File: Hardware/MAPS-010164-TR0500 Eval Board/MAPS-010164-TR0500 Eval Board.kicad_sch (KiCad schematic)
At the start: 13 parts, among them IC1 MAPS-010164-TR0500, J1 Conn_Coaxial, J2 Conn_Coaxial, J3 Conn_02x02_Top_Bottom, J4 Conn_02x02_Top_Bottom, J5 Conn_02x04_Top_Bottom, J6 Conn_Coaxial, J7 Conn_Coaxial, J8 Conn_02x02_Top_Bottom

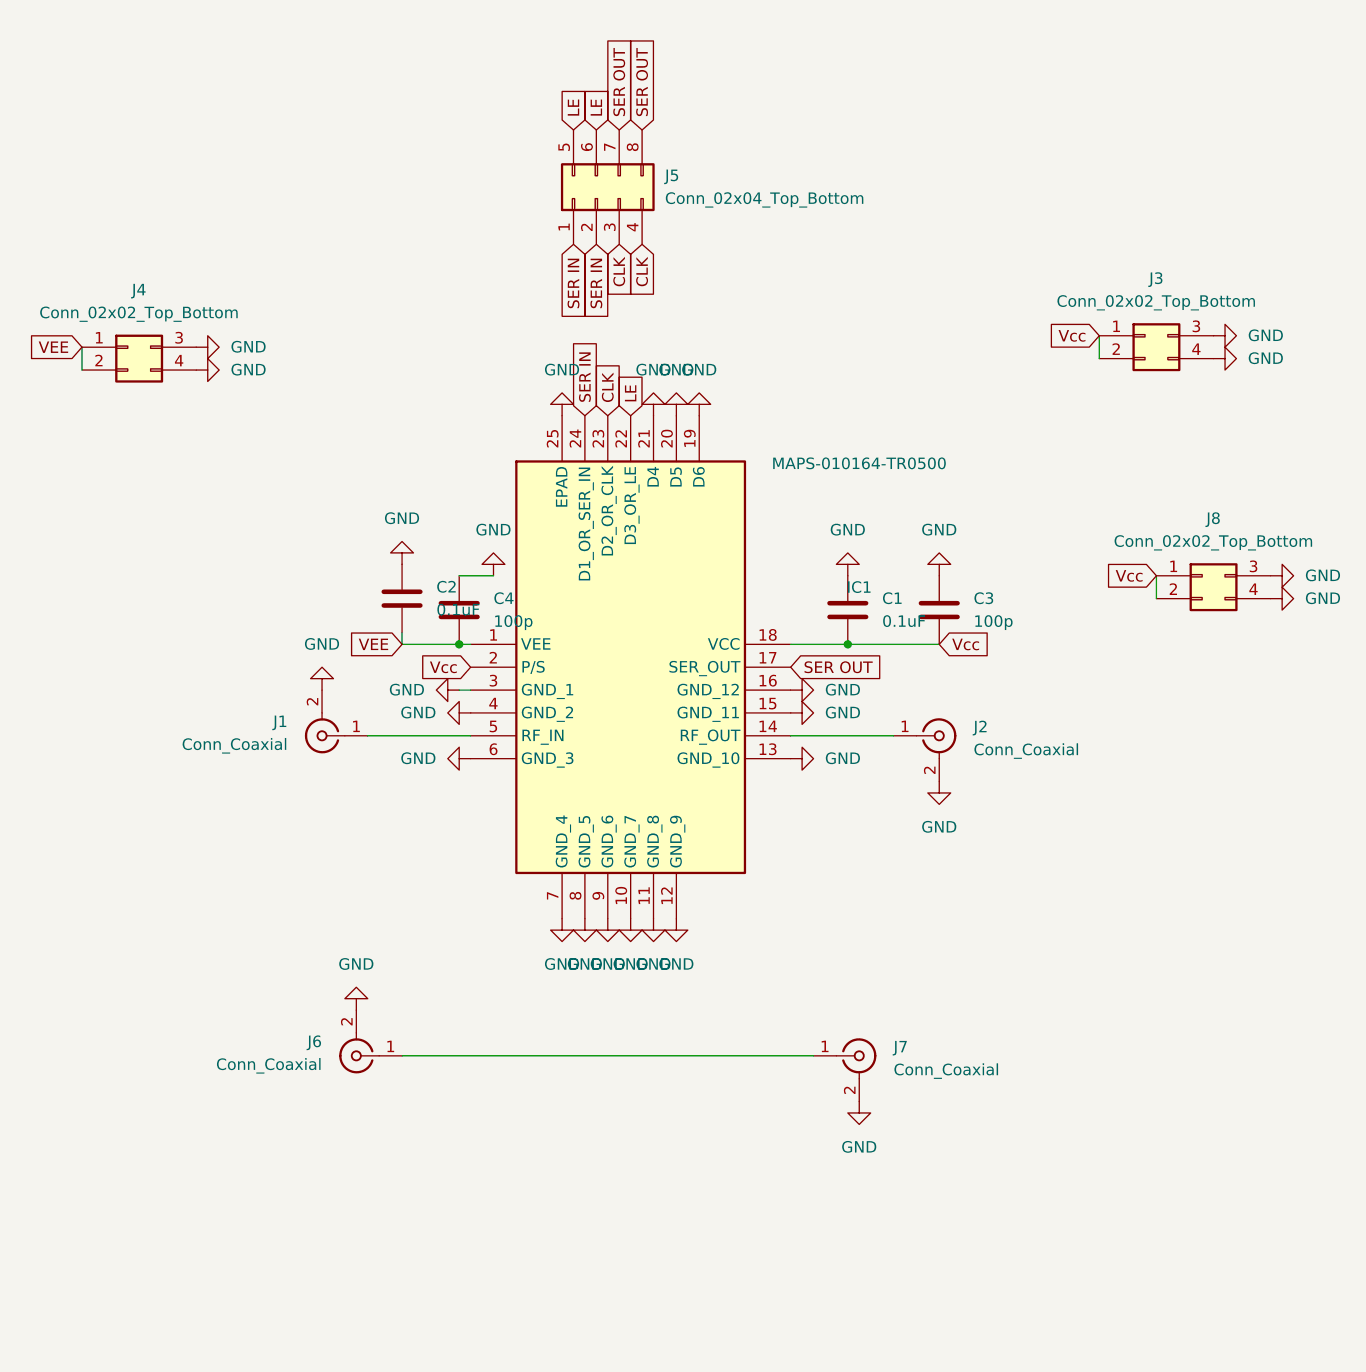
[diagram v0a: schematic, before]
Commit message: Digital Line Filtering
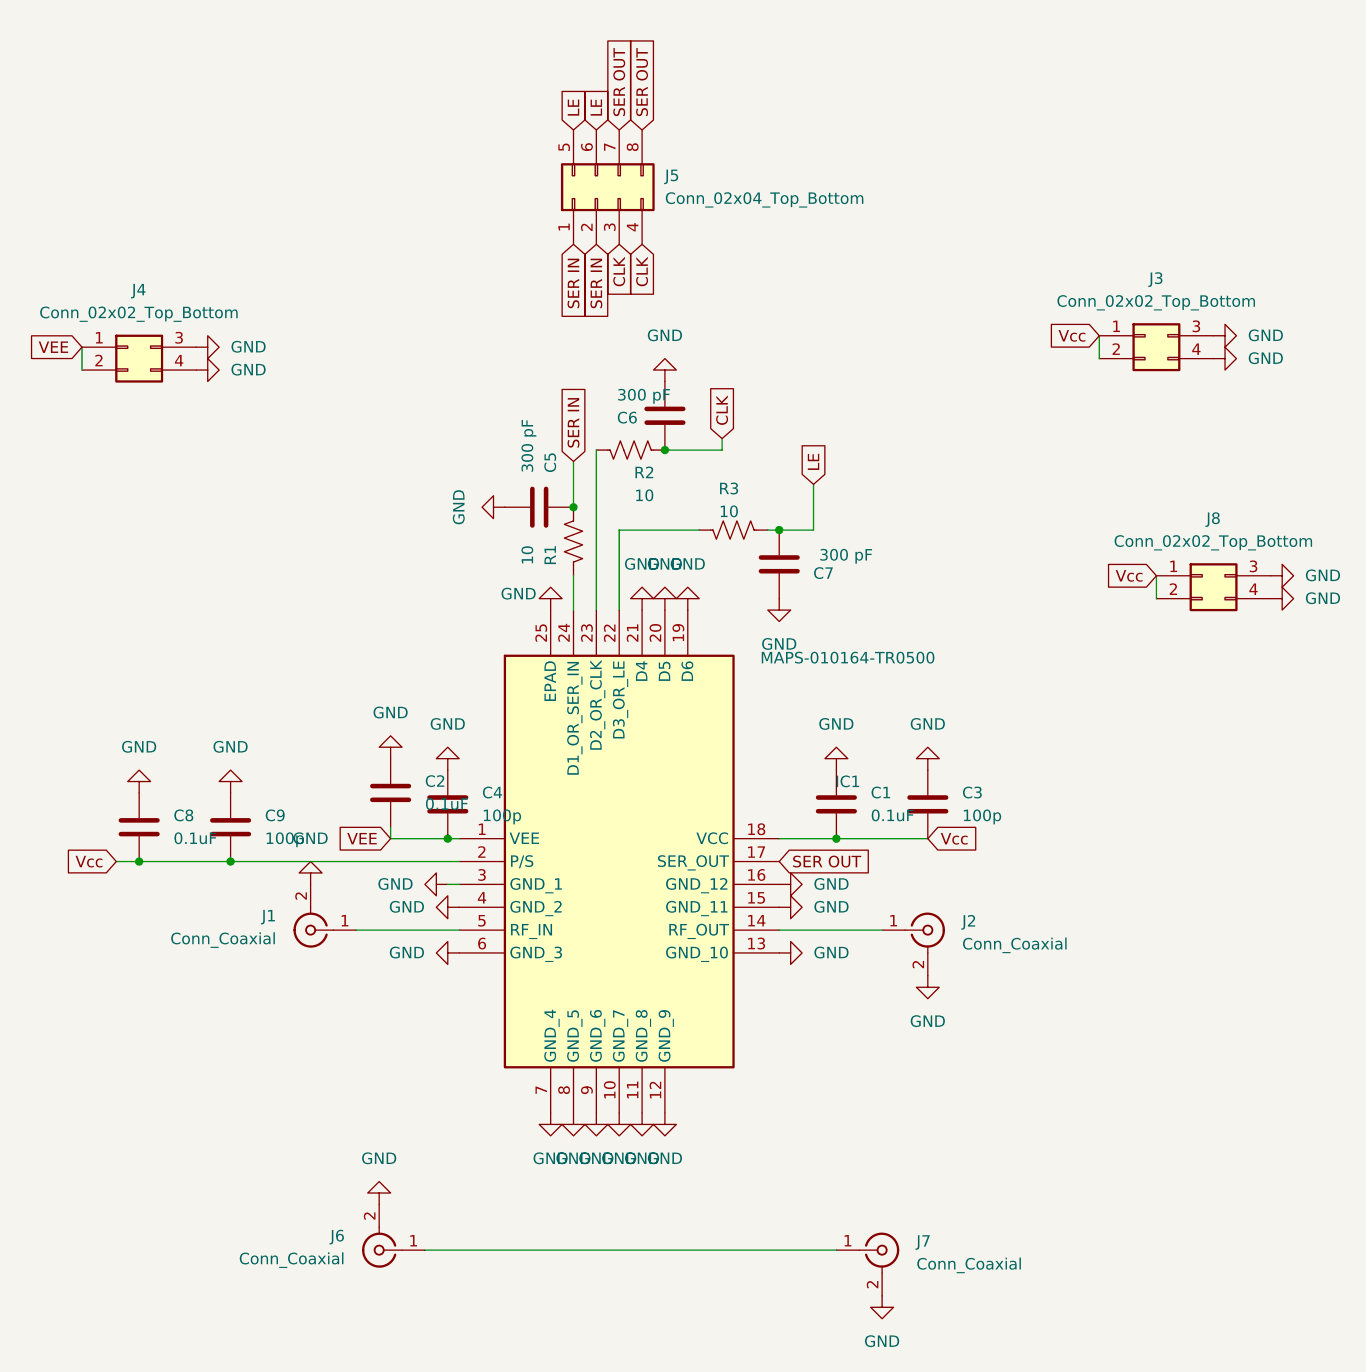
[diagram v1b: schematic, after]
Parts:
- added C5, C6, C7: 300 pF, Capacitor_SMD:C_0402_1005Metric, symbol Device:C
- added C8: 0.1uF, Capacitor_SMD:C_0402_1005Metric, symbol Device:C
- added C9: 100p, Capacitor_SMD:C_0402_1005Metric, symbol Device:C
- added R1, R2, R3: 10, Capacitor_SMD:C_0402_1005Metric, symbol Device:R_US
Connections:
- net CLK: now also C6.1, R2.1; no longer IC1.23 (D2_OR_CLK)
- net GND: now also C5.2, C6.2, C7.2, C8.1, C9.1
- net LE: now also C7.1, R3.1; no longer IC1.22 (D3_OR_LE)
- net SER IN: now also C5.1, R1.2; no longer IC1.24 (D1_OR_SER_IN)
- net Vcc: now also C8.2, C9.2
- new net: IC1.23 (D2_OR_CLK), R2.2
- new net: IC1.22 (D3_OR_LE), R3.2
- new net: IC1.24 (D1_OR_SER_IN), R1.1
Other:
- moved on the sheet: C1, C2, C3, C4, IC1, J1, J2, J6, J7

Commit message: Attenuator board. TODO: Waveguides
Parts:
- added C10: 300 pF, Capacitor_SMD:C_0402_1005Metric, symbol Device:C
- added R4: 10, Capacitor_SMD:C_0402_1005Metric, symbol Device:R_US
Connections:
- net CLK: no longer C6.1
- net GND: now also C10.2
- net LE: no longer C7.1
- net SER IN: no longer C5.1
- net SER OUT: now also R4.1; no longer IC1.17 (SER_OUT)
- net at IC1.23 (D2_OR_CLK), R2.2: now also C6.1
- net at IC1.22 (D3_OR_LE), R3.2: now also C7.1
- net at IC1.24 (D1_OR_SER_IN), R1.1: now also C5.1
- new net: C10.1, IC1.17 (SER_OUT), R4.2
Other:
- moved on the sheet: C5, C6, C7, R1, R2, R3

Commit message: DRC and header re-sizing
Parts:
- J3, J4, J8: footprint Connector_PinHeader_1.00mm:PinHeader_2x02_P1.00mm_Vertical -> Connector_PinHeader_2.00mm:PinHeader_2x02_P2.00mm_Vertical
- J5: footprint Connector_PinHeader_1.00mm:PinHeader_2x04_P1.00mm_Vertical -> Connector_PinHeader_2.00mm:PinHeader_2x04_P2.00mm_Vertical
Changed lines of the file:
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@@
 			)
 		)
-		(property "Footprint" "Connector_PinHeader_1.00mm:PinHeader_2x04_P1.00mm_Vertical"
+		(property "Footprint" "Connector_PinHeader_2.00mm:PinHeader_2x04_P2.00mm_Vertical"
 			(at 140.97 34.29 0)
 			(effects
@@
 			)
 		)
-		(property "Footprint" "Connector_PinHeader_1.00mm:PinHeader_2x02_P1.00mm_Vertical"
+		(property "Footprint" "Connector_PinHeader_2.00mm:PinHeader_2x02_P2.00mm_Vertical"
 			(at 88.9 50.8 0)
 			(effects
@@
 			)
 		)
-		(property "Footprint" "Connector_PinHeader_1.00mm:PinHeader_2x02_P1.00mm_Vertical"
+		(property "Footprint" "Connector_PinHeader_2.00mm:PinHeader_2x02_P2.00mm_Vertical"
 			(at 208.28 76.2 0)
 			(effects
@@
 			)
 		)
-		(property "Footprint" "Connector_PinHeader_1.00mm:PinHeader_2x02_P1.00mm_Vertical"
+		(property "Footprint" "Connector_PinHeader_2.00mm:PinHeader_2x02_P2.00mm_Vertical"
 			(at 201.93 49.53 0)
 			(effects
